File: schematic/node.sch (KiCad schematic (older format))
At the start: 12 parts, among them IC1 ATMEGA328P-P, P1 NRF24L01, P2 CONN_01X06, P3 CONN_01X02

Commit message: add kicad design files
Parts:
- removed C1, C4: 0.1 uF, Capacitors_ThroughHole:C_Disc_D3_P2.5, symbol C
- added C3: C, Capacitors_ThroughHole:C_Disc_D3_P2.5, symbol C
- added P4: HEADER_LEFT, Pin_Headers:Pin_Header_Straight_1x08, symbol CONN_01X08
- added P5: HEADER_RIGHT, Pin_Headers:Pin_Header_Straight_1x05, symbol CONN_01X05
- renumbered C2 to C1, C3 to C2, C5 to C4
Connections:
- net DTR: now also C3.2
- net at IC1.1 ((PCINT14/~RESET~)PC6), R1.2: now also C3.1
- net PB7: now reaches IC1.10 ((PCINT7/XTAL2/TOSC2)PB7)
- net PB7: now also P4.4 (P4)
- net PD5: now reaches IC1.11 ((PCINT21/OC0B/T1)PD5)
- net PD5: now also P4.5 (P5)
- net PD6: now reaches IC1.12 ((PCINT22/OC0A/AIN0)PD6)
- net PD6: now also P4.6 (P6)
- net PD7: now reaches IC1.13 ((PCINT23/AIN1)PD7)
- net PD7: now also P4.7 (P7)
- net PB0: now reaches IC1.14 ((PCINT0/CLKO/ICP1)PB0)
- net PB0: now also P4.8 (P8)
- net at IC1.15 ((PCINT1/OC1A)PB1): now also P1.3 (P3)
- net PC1: now reaches IC1.24 ((PCINT9/ADC1)PC1)
- net PC1: now also P5.1 (P1)
- net PC2: now reaches IC1.25 ((PCINT10/ADC2)PC2)
- net PC2: now also P5.2 (P2)
- net PC3: now reaches IC1.26 ((PCINT11/ADC3)PC3)
- net PC3: now also P5.3 (P3)
- net PC4: now reaches IC1.27 ((PCINT12/SDA/ADC4)PC4)
- net PC4: now also P5.4 (P4)
- net PC5: now reaches IC1.28 ((PCINT13/SCL/ADC5)PC5)
- net PC5: now also P5.5 (P5)
- net at P1.8 (P8): now also IC1.6 ((PCINT20/XCK/T0)PD4); no longer IC1.4 ((PCINT18/INT0)PD2)
- net PD3: now reaches IC1.5 ((PCINT19/OC2B/INT1)PD3)
- net PD3: now also P4.2 (P2)
- net PB6: now reaches IC1.9 ((PCINT6/XTAL1/TOSC1)PB6)
- net PB6: now also P4.3 (P3); no longer P1.3 (P3)
- new net PD2: IC1.4 ((PCINT18/INT0)PD2), P4.1 (P1)
- no-connect marks 14 -> 1

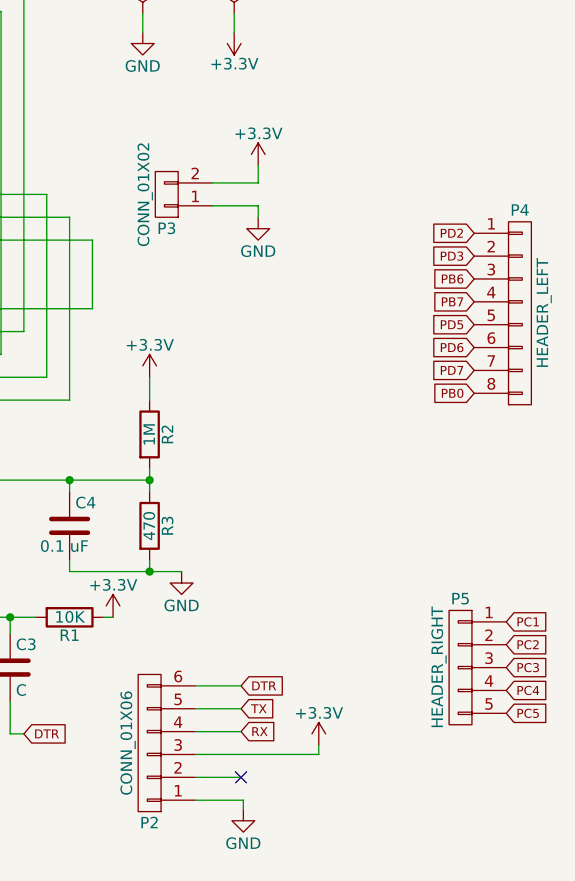
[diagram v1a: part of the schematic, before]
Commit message: refactoring in pcb layout
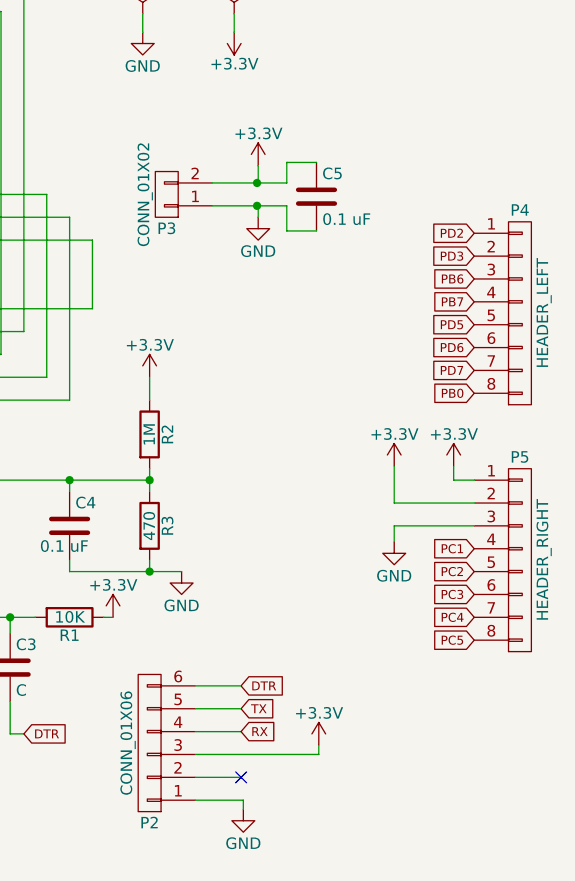
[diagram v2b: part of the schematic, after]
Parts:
- removed P5: HEADER_RIGHT, Pin_Headers:Pin_Header_Straight_1x05, symbol CONN_01X05
- added C5: 0.1 uF, Capacitors_ThroughHole:C_Disc_D3_P2.5, symbol C
- added P5: HEADER_RIGHT, Pin_Headers:Pin_Header_Straight_1x08, symbol CONN_01X08
- P1: footprint Pin_Headers:Pin_Header_Straight_2x04 -> Socket_Strips:Socket_Strip_Straight_2x04
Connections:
- net +3V3: now also C5.1, P5.1 (P1), P5.2 (P2)
- net GND: now also C5.2, P5.3 (P3)
- net PC1: now also P5.4 (P4)
- net PC2: now also P5.5 (P5)
- net PC3: now also P5.6 (P6)
- net PC4: now also P5.7 (P7)
- net PC5: now also P5.8 (P8)

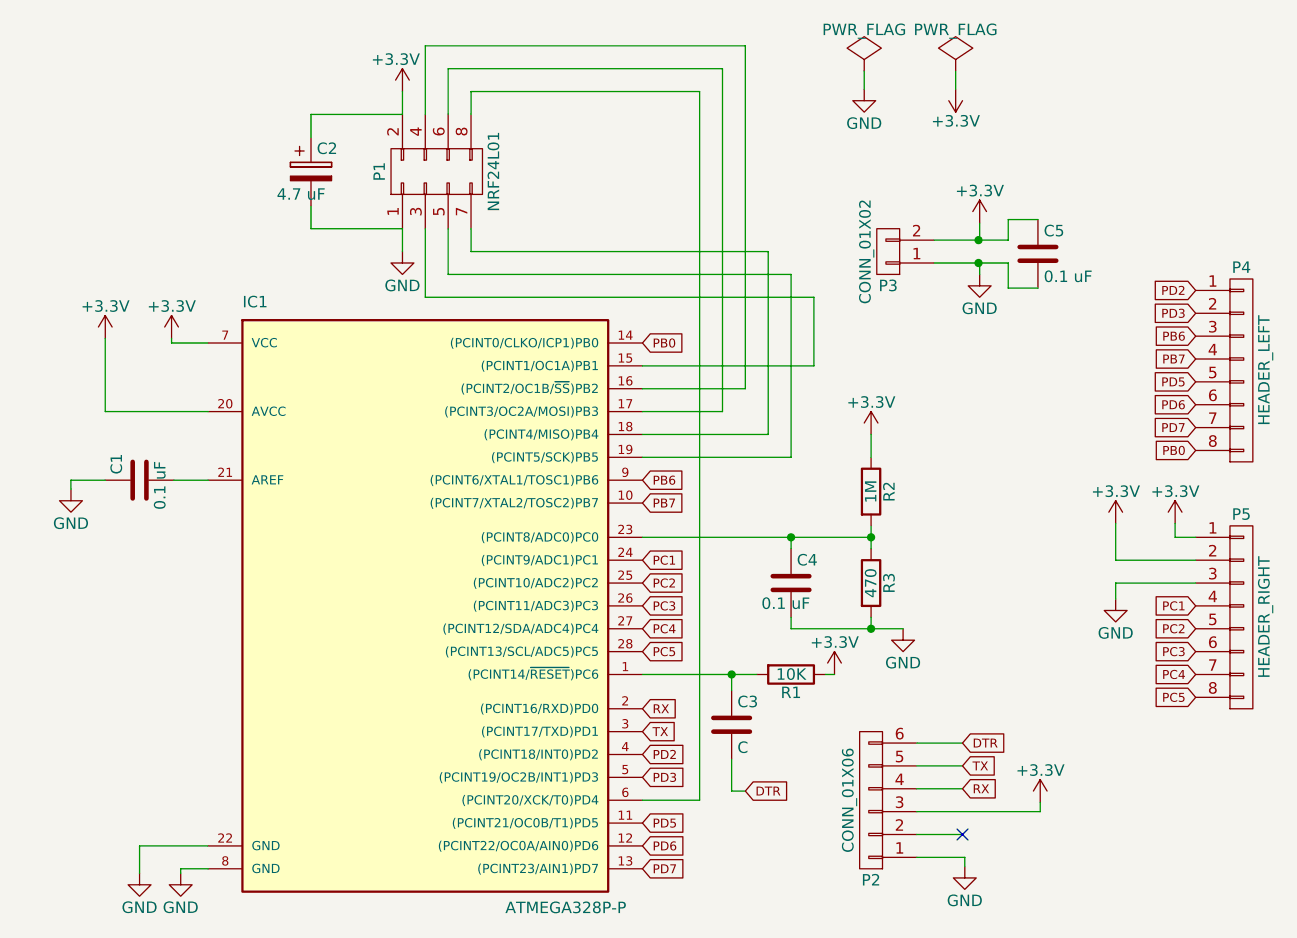
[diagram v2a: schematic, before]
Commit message: fix RF irq bug in schematic
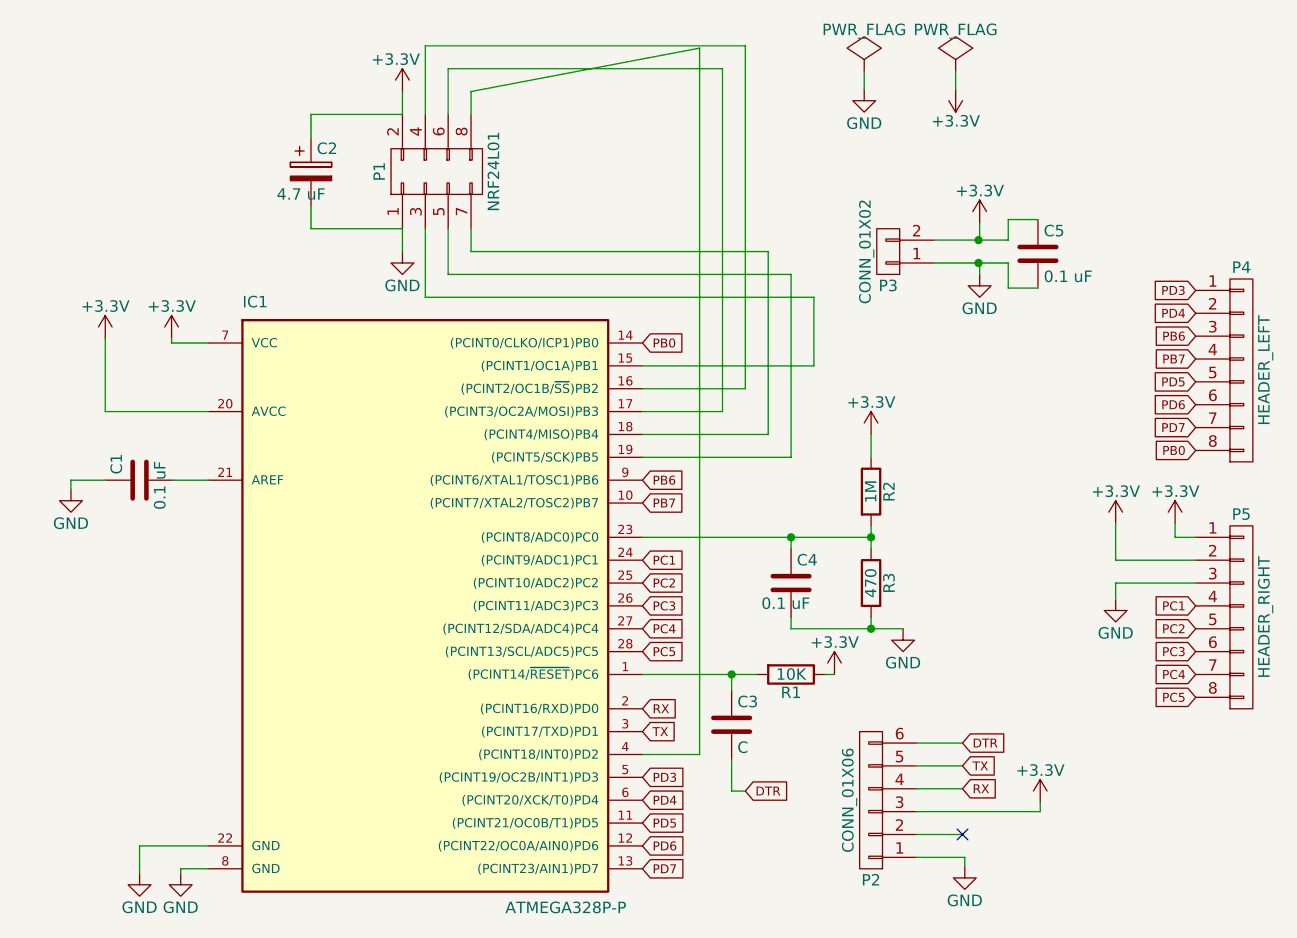
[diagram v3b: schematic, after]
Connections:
- net PD3: now also P4.1 (P1); no longer P4.2 (P2)
- net at P1.8 (P8): now also IC1.4 ((PCINT18/INT0)PD2); no longer IC1.6 ((PCINT20/XCK/T0)PD4)
- removed net PD2: IC1.4 ((PCINT18/INT0)PD2), P4.1 (P1)
- new net PD4: IC1.6 ((PCINT20/XCK/T0)PD4), P4.2 (P2)
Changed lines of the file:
@@
 Text GLabel 5550 4850 2    39   Input ~ 0
 PD7
-Text GLabel 5550 4350 2    39   Input ~ 0
-PD2
+Text GLabel 5550 4550 2    39   Input ~ 0
+PD4
 Text GLabel 7970 2320 0    39   Input ~ 0
-PD2
+PD3
 Text GLabel 7970 2420 0    39   Input ~ 0
-PD3
+PD4
 Text GLabel 7970 2520 0    39   Input ~ 0
 PB6
@@
 	4800 1550 4800 1450
 Wire Wire Line
-	4800 1450 5800 1450
-Wire Wire Line
-	5800 1450 5800 4550
+	4800 1450 5800 1260
+Wire Wire Line
+	5800 1260 5800 4350
 Wire Wire Line
 	4700 1550 4700 1350
@@
 	6300 2650 6300 2350
 Wire Wire Line
-	5800 4550 5550 4550
-Wire Wire Line
 	7880 3340 7880 3400
 Wire Wire Line
@@
 	7150 2310 7280 2310
 Connection ~ 7020 2200
+Wire Wire Line
+	5800 4350 5550 4350
 $EndSCHEMATC
